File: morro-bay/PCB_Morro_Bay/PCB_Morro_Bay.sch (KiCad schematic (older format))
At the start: 74 parts, among them J1 Conn_01x02, J2 Conn_01x04, J23 Conn_01x04, J36 SWD, J37 Conn_01x06, J38 USB_B, J39 Conn_01x06, SW3 SW_Push, U1 MCP2515-xSO, U13 V7805-2000R, U2 SN65HVD232, U3 AZ1117-3.3, U4 ATSAMD21J18A-AU, Y1 8MHz, Y2 30MHz, Y3 32.768kHz

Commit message: Even more BOM and footprints
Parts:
- C1, C2: value 22pF -> 18pF; footprint (none) -> Capacitor_SMD:C_0603_1608Metric_Pad1.05x0.95mm_HandSolder; Digikey (none) -> https://www.digikey.ca/product-detail/en/samsung-electro-me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; Part Number (none) -> CL10C180FB8NNNC
- C10, C11: value C -> 18pF; footprint (none) -> Capacitor_SMD:C_0603_1608Metric_Pad1.05x0.95mm_HandSolder; Digikey (none) -> https://www.digikey.ca/product-detail/en/samsung-electro-me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; Part Number (none) -> CL10C180FB8NNNC
- C13, C14: value C -> 9pF; footprint (none) -> Capacitor_SMD:C_0603_1608Metric_Pad1.05x0.95mm_HandSolder; Digikey (none) -> https://www.digikey.ca/product-detail/en/samsung-electro-me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; Part Number (none) -> CL10C090CB8NNNC
- F1: footprint (none) -> PCB_Morro_Bay:Fuse_Littelfuse_0154003.DR
- FB1: footprint (none) -> PCB_Morro_Bay:Ferrite_Laird_HI2220P701R-10; Digikey 240-2428-1-ND -> https://www.digikey.ca/products/en?keywords=240-2428-1-ND; Part Number (none) -> HI2220P701R-10
- J38: footprint (none) -> Connector_USB:USB_B_OST_USB-B1HSxx_Horizontal; Digikey (none) -> https://www.digikey.ca/product-detail/en/cui-devices/UJ2-BH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; Part Number (none) -> UJ2-BH-1-TH
- R1, R2, R3, R4, R5, R7, R72, R8: footprint (none) -> Resistor_SMD:R_0603_1608Metric_Pad1.05x0.95mm_HandSolder; Digikey (none) -> https://www.digikey.ca/product-detail/en/stackpole-electron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; Part Number (none) -> RMCF0603FT10K0
- R116: value 500 -> 470; footprint (none) -> Resistor_SMD:R_0603_1608Metric_Pad1.05x0.95mm_HandSolder; Digikey (none) -> https://www.digikey.ca/product-detail/en/stackpole-electron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; Part Number (none) -> RMCF0603FT470R
- R117: value 500 -> 470; footprint (none) -> Resistor_SMD:R_0603_1608Metric_Pad1.05x0.95mm_HandSolder; Digikey (none) -> https://www.digikey.ca/product-detail/en/stackpole-electron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; RMCF0603FT470R (none) -> RMCF0603FT470R
- R118, R119, R70, R71: footprint (none) -> Resistor_SMD:R_0603_1608Metric_Pad1.05x0.95mm_HandSolder; Digikey (none) -> https://www.digikey.ca/product-detail/en/rohm-semiconductor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; Part Number (none) -> ESR03EZPJ331
- R6: footprint (none) -> Resistor_SMD:R_0603_1608Metric_Pad1.05x0.95mm_HandSolder; Digikey (none) -> https://www.digikey.ca/product-detail/en/stackpole-electron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; Part Number (none) -> RMCF0603JT120R
- R69: value 600 -> 620; footprint (none) -> Resistor_SMD:R_0603_1608Metric_Pad1.05x0.95mm_HandSolder; Digikey (none) -> https://www.digikey.ca/product-detail/en/stackpole-electron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; Part Number (none) -> RMCF0603FT620R
- R73: footprint (none) -> Resistor_SMD:R_0603_1608Metric_Pad1.05x0.95mm_HandSolder; Digikey (none) -> https://www.digikey.ca/product-detail/en/stackpole-electron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; Part Number (none) -> RMCF0603JJ1K00
- U13: footprint (none) -> Converter_DCDC:Converter_DCDC_RECOM_R-78HB-0.5L_THT; Digikey (none) -> https://www.digikey.ca/products/en?keywords=V7805-2000R; Part Number (none) -> V7805-2000R
- U3: footprint (none) -> Package_TO_SOT_SMD:SOT-223-3_TabPin2; Digikey (none) -> https://www.digikey.ca/product-detail/en/diodes-incorporate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; Part Number (none) -> AZ1117IH-3.3TRG1
- Y1: footprint (none) -> Crystal:Crystal_SMD_HC49-SD_HandSoldering; Digikey (none) -> https://www.digikey.ca/product-detail/en/abracon-llc/ABLS2-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; Part Number (none) -> ABLS2-8.000MHZ-D4Y-T
- Y2: footprint (none) -> Crystal:Crystal_SMD_HC49-SD_HandSoldering; Digikey (none) -> https://www.digikey.ca/product-detail/en/abracon-llc/ABLS2-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; Part Number (none) -> ABLS2-30.000MHZ-D4YF-T
- Y3: footprint (none) -> Crystal:Crystal_SMD_SeikoEpson_MC146-4Pin_6.7x1.5mm_HandSoldering; Digikey (none) -> https://www.digikey.ca/product-detail/en/epson/MC-146-32-76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; Part Number (none) -> MC-146 32.7680KA-AC0: ROHS
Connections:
- no-connect marks 3 -> 5
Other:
- note added: "TODO:\n-INAMPs\n-All those fucking resistors"
- note removed: "TODO:\n-Check ADC AINCOM\n-INAMPs"

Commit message: BOM BOM BOM BOM baBOM BOM baBOM...
(Imperial march)
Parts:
- removed J1: Conn_01x02, symbol Connector_Generic:Conn_01x02
- added J1: POWER, Connector_Molex:Molex_Micro-Fit_3.0_43045-0400_2x02_P3.00mm_Horizontal, symbol Connector_Generic:Conn_01x04
- D21, D22: footprint (none) -> LED_SMD:LED_0603_1608Metric_Castellated; Digikey (none) -> https://www.digikey.ca/product-detail/en/w%C3%BCrth-elektro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; Part Number (none) -> 150060VS75000
- D35, D36: footprint (none) -> LED_SMD:LED_0603_1608Metric_Castellated; Digikey (none) -> https://www.digikey.ca/product-detail/en/lite-on-inc/LTST-C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; Part Number (none) -> LTST-C191KFKT
- D37: footprint (none) -> LED_SMD:LED_0603_1608Metric_Castellated; Digikey (none) -> https://www.digikey.ca/product-detail/en/w%C3%BCrth-elektro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; Part Number (none) -> 150060SS75000
- D38: footprint (none) -> LED_SMD:LED_0603_1608Metric_Castellated; Digikey (none) -> https://www.digikey.ca/product-detail/en/w%C3%BCrth-elektro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; Part Number (none) -> 150060YS75000
- J2: value Conn_01x04 -> CAN
- J23: value Conn_01x04 -> POWER_OUT
- J37: value Conn_01x06 -> GPIO
- J39: value Conn_01x06 -> ESERCOM
- JP1: value Jumper_NC_Small -> CAN_TERM; footprint (none) -> Jumper:SolderJumper-2_P1.3mm_Open_RoundedPad1.0x1.5mm
- R117: Part Number (none) -> RMCF0603FT470R; RMCF0603FT470R RMCF0603FT470R -> (none)
- SW3: value SW_Push -> RESET; footprint (none) -> Button_Switch_SMD:SW_SPST_TL3305A; Digikey (none) -> https://www.digikey.ca/en/products/detail/e-switch/TL3305AF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; Part Number (none) -> TL3305AF160QG
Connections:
- net +3V3: now also J39.6 (Pin_6)
- net +5V: no longer J39.6 (Pin_6)
- net GND: now also J1.1 (Pin_1), J1.2 (Pin_2)
- net VIN: now also J1.3 (Pin_3), J1.4 (Pin_4)
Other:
- note added: "TODO:\n-Distance sensors?\n-Connector footprints"
- note removed: "TODO:\n-INAMPs\n-All those fucking resistors"
- moved on the sheet: J23

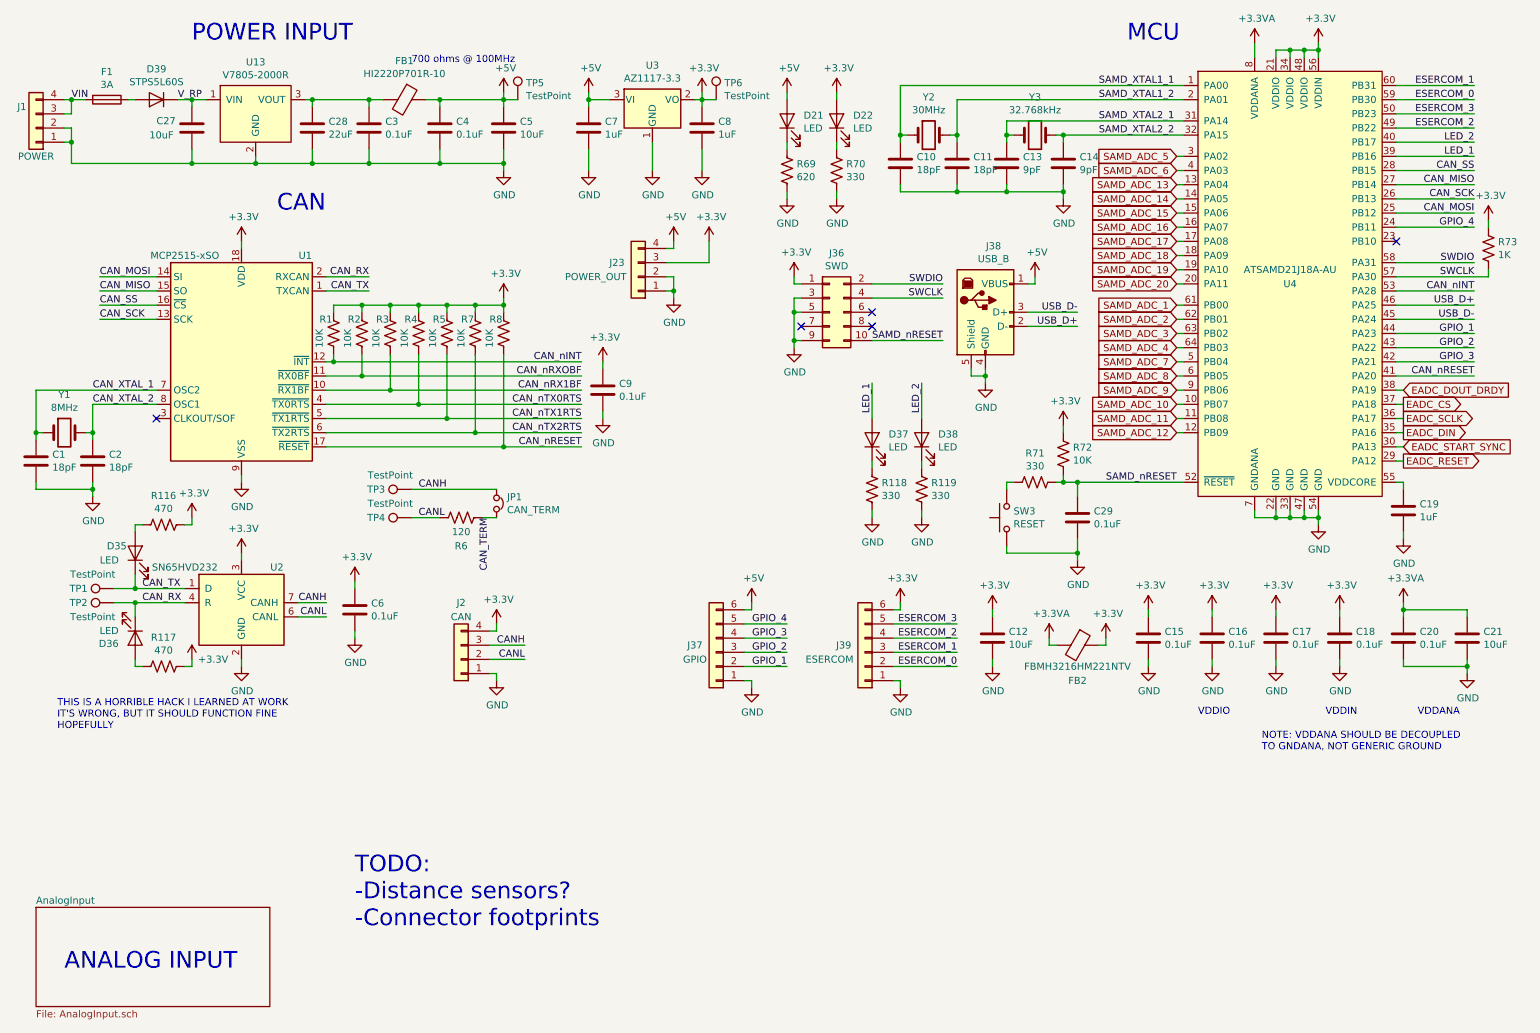
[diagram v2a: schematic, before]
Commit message: Start layout, finish BOM
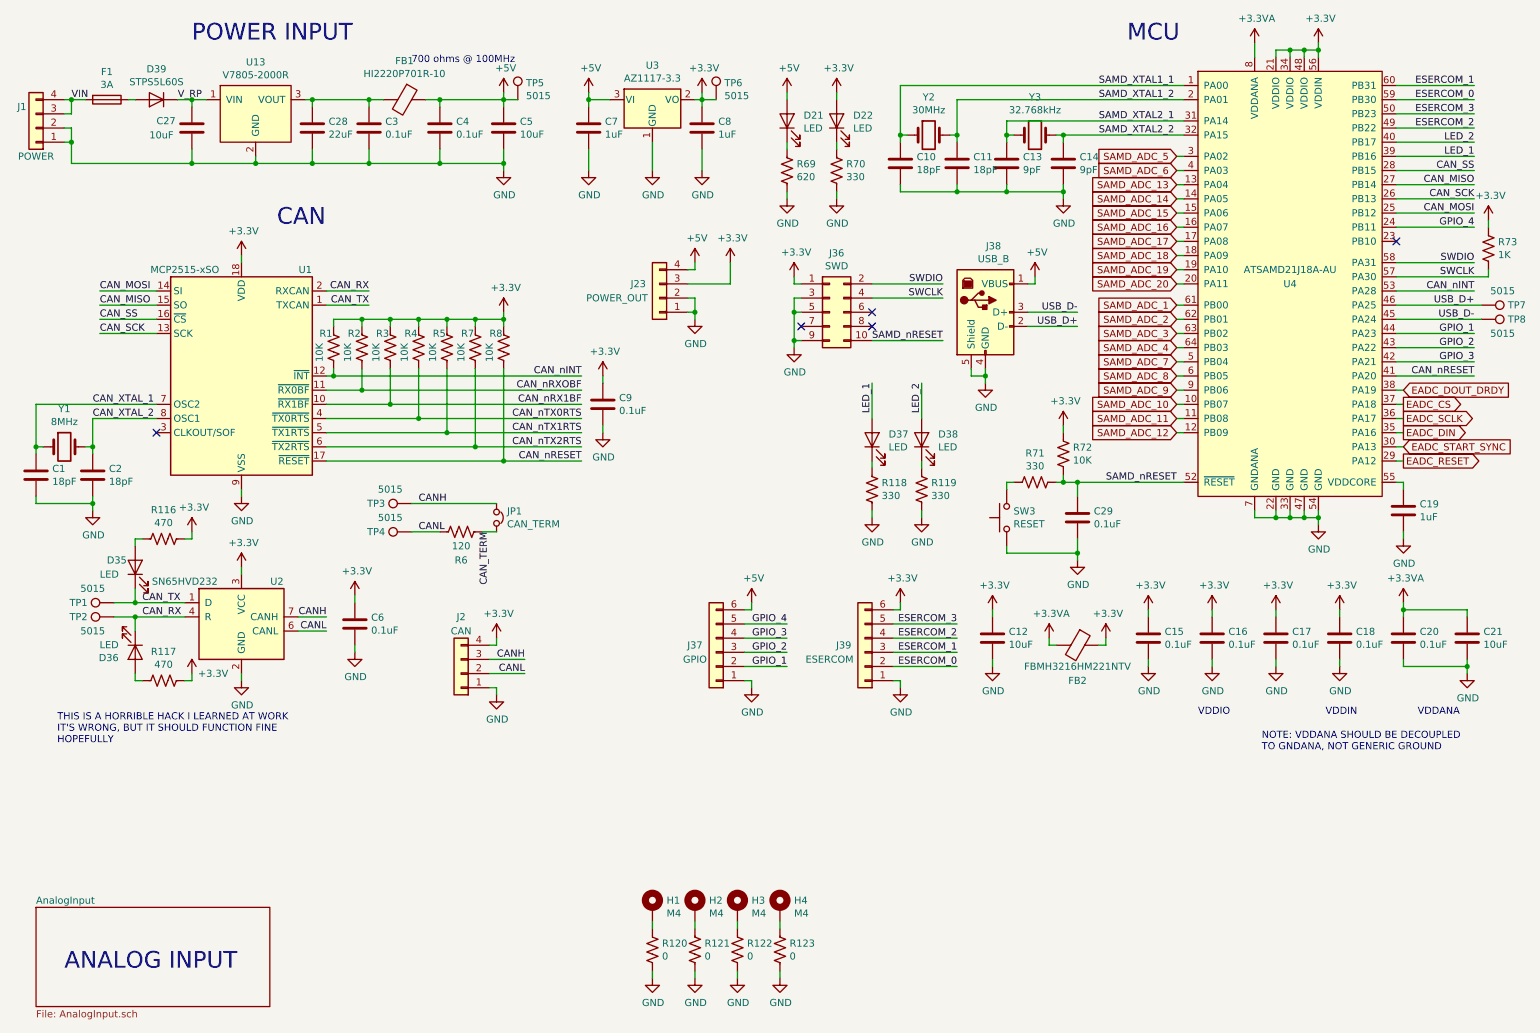
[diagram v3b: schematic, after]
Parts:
- added H1, H2, H3, H4: M4, MountingHole:MountingHole_4.3mm_M4_Pad, symbol Mechanical:MountingHole_Pad
- added R120, R121, R122, R123: 0, Resistor_SMD:R_0805_2012Metric_Pad1.15x1.40mm_HandSolder, symbol Device:R_US
- added TP7, TP8: 5015, TestPoint:TestPoint_Keystone_5015_Micro-Minature, symbol Connector:TestPoint
- J2: footprint (none) -> PCB_Morro_Bay:Connector_Molex_SL_4POS_0705510038; Digikey (none) -> https://www.digikey.ca/product-detail/en/molex/0705510038/W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; Part Number (none) -> 0705510038
- J23: footprint (none) -> Connector_Molex:Molex_Micro-Fit_3.0_43045-0400_2x02_P3.00mm_Horizontal
- J36: footprint (none) -> PCB_Morro_Bay:Connector_TE_5103308-1; Digikey (none) -> https://www.digikey.ca/product-detail/en/te-connectivity-am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; Part Number (none) -> 5103308-1
- J37, J39: footprint (none) -> PCB_Morro_Bay:Connector_Molex_SL_6POS_0705510005; Digikey (none) -> https://www.digikey.ca/en/products/detail/molex/0705510005/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; Part Number (none) -> 0705510005
- TP1, TP2, TP3, TP4, TP5, TP6: value TestPoint -> 5015; footprint (none) -> TestPoint:TestPoint_Keystone_5015_Micro-Minature; Digikey (none) -> https://www.digikey.ca/product-detail/en/keystone-electroni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; Part Number (none) -> 5015
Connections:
- net GND: now also R120.2, R121.2, R122.2, R123.2
- net USB_D+: now also TP7.1
- net USB_D-: now also TP8.1
- new net: H1.1, R120.1
- new net: H2.1, R121.1
- new net: H3.1, R122.1
- new net: H4.1, R123.1
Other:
- note removed: "TODO:\n-Distance sensors?\n-Connector footprints"
- moved on the sheet: C1, C2, C6, C9, D35, D36, J2, J23, JP1, R1, R116, R117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
